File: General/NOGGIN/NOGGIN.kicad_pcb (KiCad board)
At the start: 4 copper layers, 31.2 x 34 mm, 60 parts, among them J1 CAN, J2 CAN, J3 SWD_UART, J4 Extra, J5 I2C, J6 UART, J7 DAC1, J8 DAC2, J9 MOTOR, SW1 DBG2, SW2 DBG1, SW3 RST, U1 STM32F072CBUx, U2 AZ1117-3.3, U3 ATA6561, U4 ACS70331, U5 ACS70331, U6 DRV8871DDA

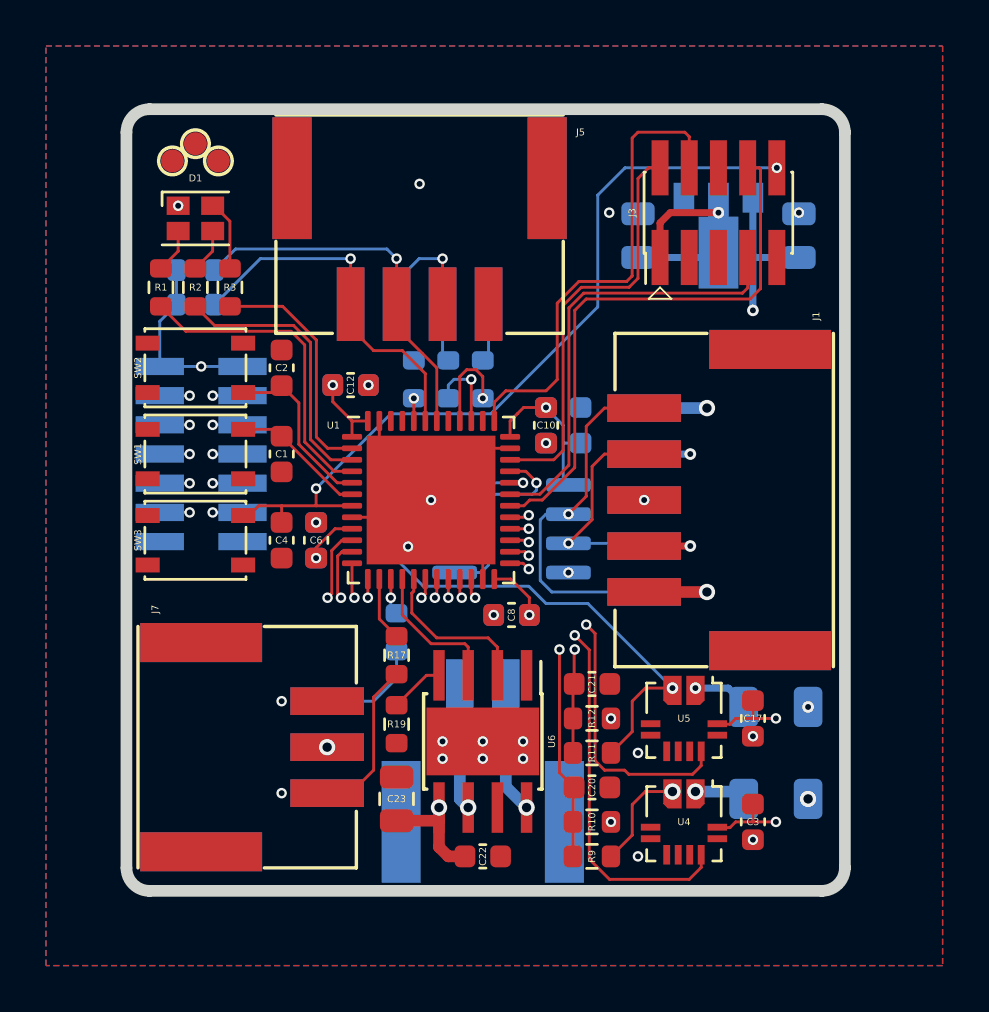
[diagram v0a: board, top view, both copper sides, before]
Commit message: convert to kicad 6
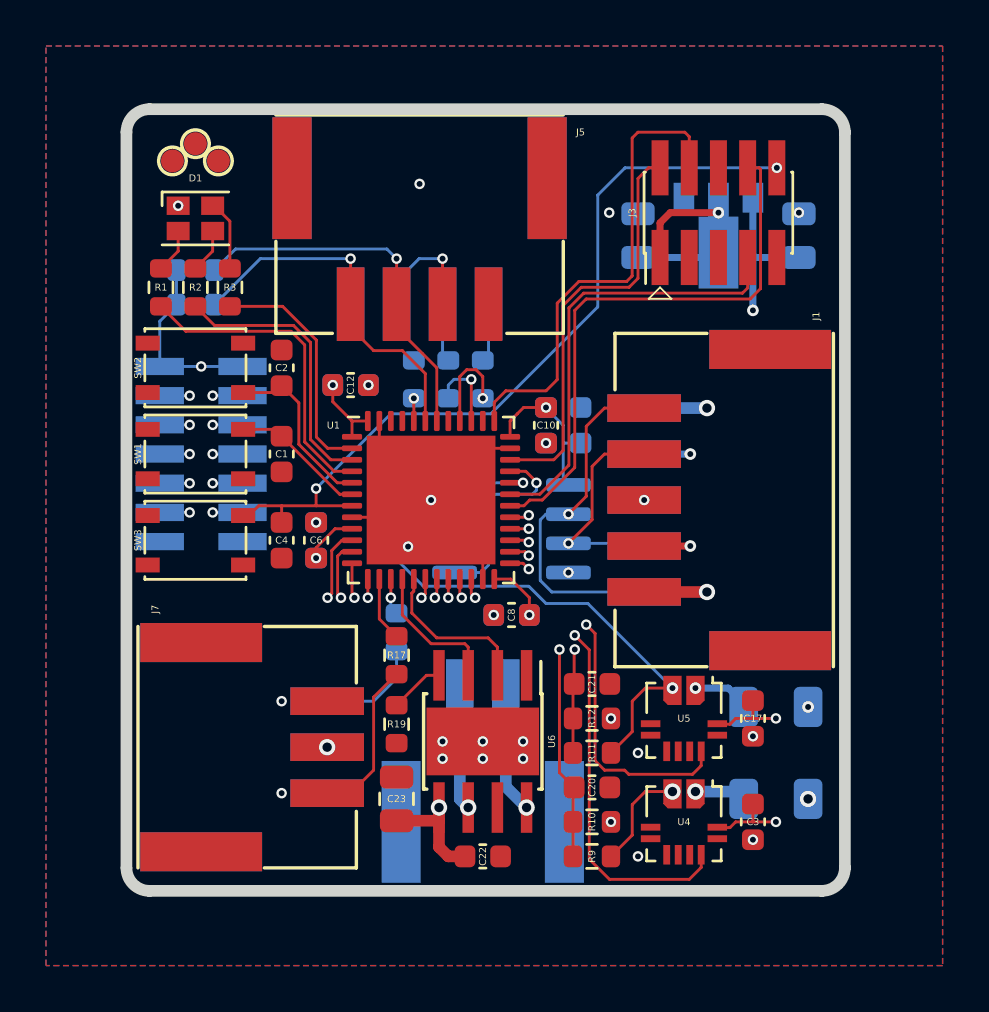
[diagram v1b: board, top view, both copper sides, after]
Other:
- net class BigPower removed
- net class Default removed
- net class SmallPower removed
